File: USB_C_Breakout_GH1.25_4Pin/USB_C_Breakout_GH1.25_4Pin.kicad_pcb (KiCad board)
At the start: 2 copper layers, 20.3 x 15.2 mm, 7 parts, among them J1 USB_C_Receptacle_USB2.0, J2 Conn_01x04_MountingPin

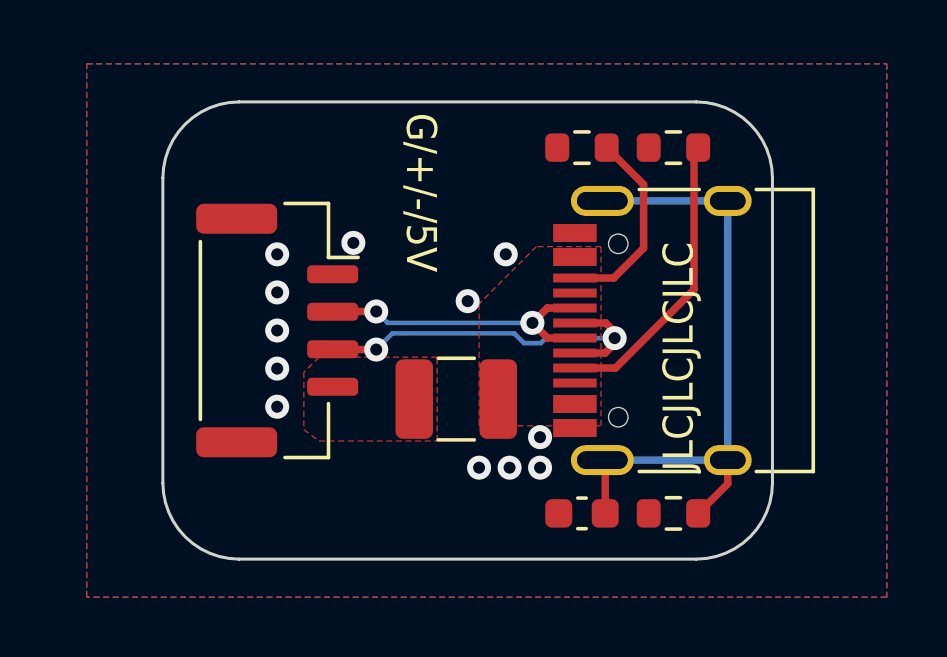
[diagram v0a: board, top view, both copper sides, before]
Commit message: change USB pin sequence to make it more universal
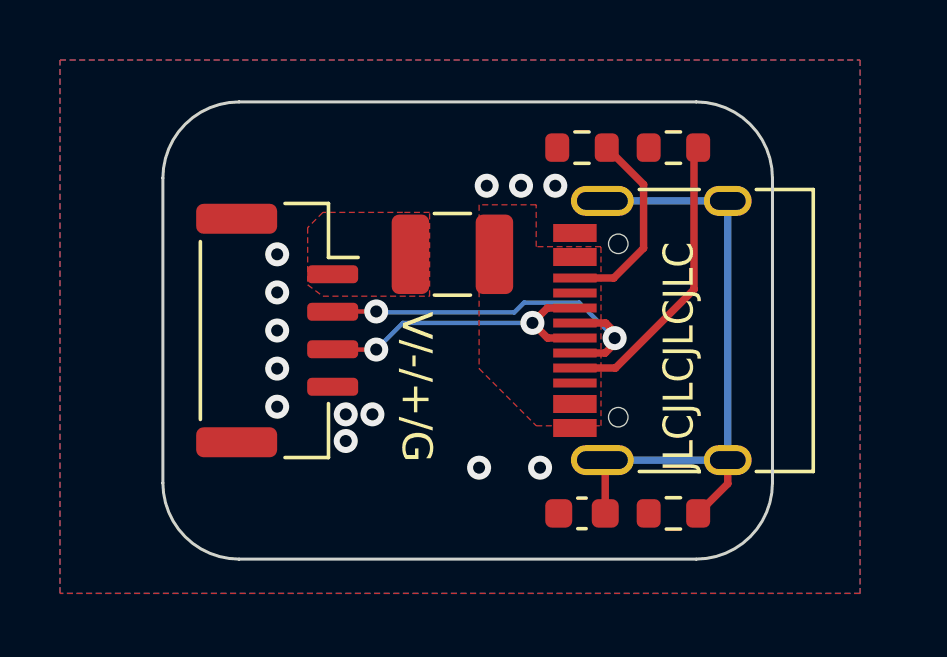
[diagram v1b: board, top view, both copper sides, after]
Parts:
- moved F1 4.83 mm to (121.4, 73.7)
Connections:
- J2 pad 1: GND -> +5V
- J2 pad 2: /USB_DP -> /USB_DM
- J2 pad 3: /USB_DM -> /USB_DP
- J2 pad 4: +5V -> GND
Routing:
- net GND: vias 12 -> 13
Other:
- board text added: "V/-/+/G"
- board text removed: "G/+/-/5V"
